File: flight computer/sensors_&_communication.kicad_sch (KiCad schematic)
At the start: 30 parts, among them IC2 114993390, IC3 ADXL375BCCZ-RL, J22 SMA-J-P-H-ST-EM1, J23 SMA-J-P-H-ST-EM1, U10 MAX-M10S-00B, U8 BMP581, U9 BNO086

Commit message: General progress on the PCB
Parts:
- C42, C43, C44, C45, C46, C47, C48, C49, C50, C51, C52, C53, C54: footprint Capacitor_SMD:C_0805_2012Metric_Pad1.18x1.45mm_HandSolder -> Capacitor_SMD:C_0603_1608Metric_Pad1.08x0.95mm_HandSolder
- R39, R40, R41, R42, R43, R44: footprint Resistor_SMD:R_0805_2012Metric_Pad1.20x1.40mm_HandSolder -> Resistor_SMD:R_0603_1608Metric_Pad0.98x0.95mm_HandSolder
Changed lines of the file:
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@@
 			)
 		)
-		(property "Footprint" "Capacitor_SMD:C_0805_2012Metric_Pad1.18x1.45mm_HandSolder"
+		(property "Footprint" "Capacitor_SMD:C_0603_1608Metric_Pad1.08x0.95mm_HandSolder"
 			(at 162.2552 53.34 0)
 			(hide yes)
@@
 			)
 		)
-		(property "Footprint" "Capacitor_SMD:C_0805_2012Metric_Pad1.18x1.45mm_HandSolder"
+		(property "Footprint" "Capacitor_SMD:C_0603_1608Metric_Pad1.08x0.95mm_HandSolder"
 			(at 131.1148 38.1 0)
 			(hide yes)
@@
 			)
 		)
-		(property "Footprint" "Resistor_SMD:R_0805_2012Metric_Pad1.20x1.40mm_HandSolder"
+		(property "Footprint" "Resistor_SMD:R_0603_1608Metric_Pad0.98x0.95mm_HandSolder"
 			(at 33.02 41.148 90)
 			(hide yes)
@@
 			)
 		)
-		(property "Footprint" "Capacitor_SMD:C_0805_2012Metric_Pad1.18x1.45mm_HandSolder"
+		(property "Footprint" "Capacitor_SMD:C_0603_1608Metric_Pad1.08x0.95mm_HandSolder"
 			(at 119.6848 38.1 0)
 			(hide yes)
@@
 			)
 		)
-		(property "Footprint" "Resistor_SMD:R_0805_2012Metric_Pad1.20x1.40mm_HandSolder"
+		(property "Footprint" "Resistor_SMD:R_0603_1608Metric_Pad0.98x0.95mm_HandSolder"
 			(at 67.31 136.652 90)
 			(hide yes)
@@
 			)
 		)
-		(property "Footprint" "Capacitor_SMD:C_0805_2012Metric_Pad1.18x1.45mm_HandSolder"
+		(property "Footprint" "Capacitor_SMD:C_0603_1608Metric_Pad1.08x0.95mm_HandSolder"
 			(at 173.6852 53.34 0)
 			(hide yes)
@@
 			)
 		)
-		(property "Footprint" "Resistor_SMD:R_0805_2012Metric_Pad1.20x1.40mm_HandSolder"
+		(property "Footprint" "Resistor_SMD:R_0603_1608Metric_Pad0.98x0.95mm_HandSolder"
 			(at 33.02 43.688 90)
 			(hide yes)
@@
 			)
 		)
-		(property "Footprint" "Capacitor_SMD:C_0805_2012Metric_Pad1.18x1.45mm_HandSolder"
+		(property "Footprint" "Capacitor_SMD:C_0603_1608Metric_Pad1.08x0.95mm_HandSolder"
 			(at 98.7552 63.5 0)
 			(hide yes)
@@
 			)
 		)
-		(property "Footprint" "Resistor_SMD:R_0805_2012Metric_Pad1.20x1.40mm_HandSolder"
+		(property "Footprint" "Resistor_SMD:R_0603_1608Metric_Pad0.98x0.95mm_HandSolder"
 			(at 101.6 46.482 90)
 			(hide yes)
@@
 			)
 		)
-		(property "Footprint" "Capacitor_SMD:C_0805_2012Metric_Pad1.18x1.45mm_HandSolder"
+		(property "Footprint" "Capacitor_SMD:C_0603_1608Metric_Pad1.08x0.95mm_HandSolder"
 			(at 177.4952 101.6 0)
 			(hide yes)
@@
 			)
 		)
-		(property "Footprint" "Capacitor_SMD:C_0805_2012Metric_Pad1.18x1.45mm_HandSolder"
+		(property "Footprint" "Capacitor_SMD:C_0603_1608Metric_Pad1.08x0.95mm_HandSolder"
 			(at 23.1648 97.79 0)
 			(hide yes)
@@
 			)
 		)
-		(property "Footprint" "Capacitor_SMD:C_0805_2012Metric_Pad1.18x1.45mm_HandSolder"
+		(property "Footprint" "Capacitor_SMD:C_0603_1608Metric_Pad1.08x0.95mm_HandSolder"
 			(at 82.2452 97.79 0)
 			(hide yes)
@@
 			)
 		)
-		(property "Footprint" "Resistor_SMD:R_0805_2012Metric_Pad1.20x1.40mm_HandSolder"
+		(property "Footprint" "Resistor_SMD:R_0603_1608Metric_Pad0.98x0.95mm_HandSolder"
 			(at 101.6 41.148 90)
 			(hide yes)
@@
 			)
 		)
-		(property "Footprint" "Capacitor_SMD:C_0805_2012Metric_Pad1.18x1.45mm_HandSolder"
+		(property "Footprint" "Capacitor_SMD:C_0603_1608Metric_Pad1.08x0.95mm_HandSolder"
 			(at 164.7952 101.6 0)
 			(hide yes)
@@
 			)
 		)
-		(property "Footprint" "Capacitor_SMD:C_0805_2012Metric_Pad1.18x1.45mm_HandSolder"
+		(property "Footprint" "Capacitor_SMD:C_0603_1608Metric_Pad1.08x0.95mm_HandSolder"
 			(at 51.7652 146.05 0)
 			(hide yes)
@@
 			)
 		)
-		(property "Footprint" "Capacitor_SMD:C_0805_2012Metric_Pad1.18x1.45mm_HandSolder"
+		(property "Footprint" "Capacitor_SMD:C_0603_1608Metric_Pad1.08x0.95mm_HandSolder"
 			(at 94.9452 97.79 0)
 			(hide yes)
@@
 			)
 		)
-		(property "Footprint" "Capacitor_SMD:C_0805_2012Metric_Pad1.18x1.45mm_HandSolder"
+		(property "Footprint" "Capacitor_SMD:C_0603_1608Metric_Pad1.08x0.95mm_HandSolder"
 			(at 108.2548 38.1 0)
 			(hide yes)
@@
 			)
 		)
-		(property "Footprint" "Capacitor_SMD:C_0805_2012Metric_Pad1.18x1.45mm_HandSolder"
+		(property "Footprint" "Capacitor_SMD:C_0603_1608Metric_Pad1.08x0.95mm_HandSolder"
 			(at 150.8252 53.34 0)
 			(hide yes)
@@
 			)
 		)
-		(property "Footprint" "Resistor_SMD:R_0805_2012Metric_Pad1.20x1.40mm_HandSolder"
+		(property "Footprint" "Resistor_SMD:R_0603_1608Metric_Pad0.98x0.95mm_HandSolder"
 			(at 33.02 38.608 90)
 			(hide yes)

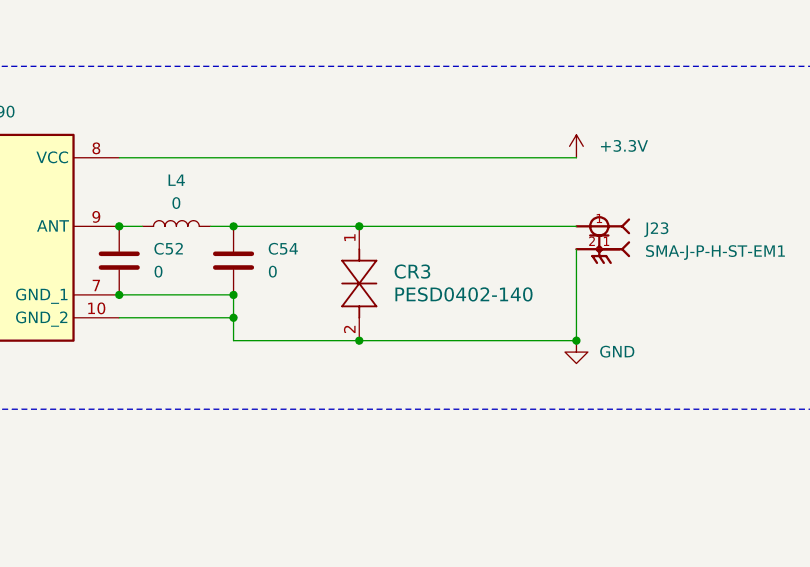
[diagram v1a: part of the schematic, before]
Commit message: Microcontroller power complete
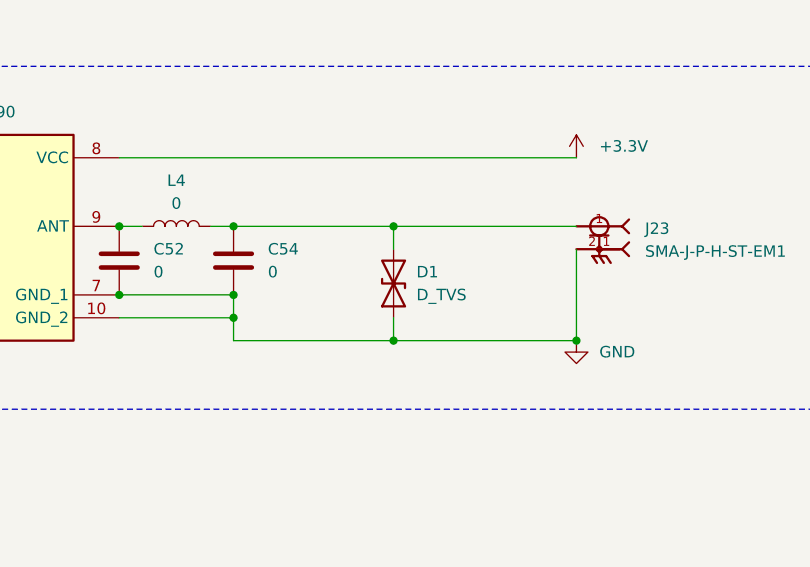
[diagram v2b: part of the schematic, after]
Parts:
- removed CR3: PESD0402-140, Inductor_SMD:L_0402_1005Metric_Pad0.77x0.64mm_HandSolder, symbol Snapeda:PESD0402-140
- added D1: D_TVS, Diode_SMD:D_0603_1608Metric_Pad1.05x0.95mm_HandSolder, symbol Device:D_TVS
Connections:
- net GND: now also D1.1 (A1)
- net at C54.1, J23.1, L4.2: now also D1.2 (A2)
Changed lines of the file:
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@@
 	)
 	(junction
-		(at 190.5 106.68)
-		(diameter 0)
-		(color 0 0 0 0)
-	)
-	(junction
 		(at 124.46 165.1)
 		(diameter 0)
@@
 	)
 	(junction
-		(at 190.5 93.98)
-		(diameter 0)
-		(color 0 0 0 0)
-	)
-	(junction
 		(at 21.59 137.16)
 		(diameter 0)
@@
 	)
 	(junction
+		(at 194.31 106.68)
+		(diameter 0)
+		(color 0 0 0 0)
+	)
+	(junction
 		(at 149.86 43.18)
 		(diameter 0)
@@
 	)
 	(junction
+		(at 194.31 93.98)
+		(diameter 0)
+		(color 0 0 0 0)
+	)
+	(junction
 		(at 109.22 30.48)
 		(diameter 0)
@@
 		)
 	)
+	(wire
+		(pts
+			(xy 194.31 104.14) (xy 194.31 106.68)
+		)
+		(stroke
+			(width 0)
+			(type default)
+		)
+	)
 	(polyline
 		(pts
@@
 	(wire
 		(pts
+			(xy 194.31 93.98) (xy 194.31 96.52)
+		)
+		(stroke
+			(width 0)
+			(type default)
+		)
+	)
+	(wire
+		(pts
 			(xy 248.92 45.72) (xy 233.68 45.72)
 		)
@@
 	(wire
 		(pts
-			(xy 190.5 106.68) (xy 214.63 106.68)
+			(xy 176.53 106.68) (xy 194.31 106.68)
 		)
 		(stroke
@@
 		)
 	)
+	(wire
+		(pts
+			(xy 194.31 93.98) (xy 214.63 93.98)
+		)
+		(stroke
+			(width 0)
+			(type default)
+		)
+	)
 	(polyline
 		(pts
@@
 	(wire
 		(pts
-			(xy 176.53 93.98) (xy 190.5 93.98)
+			(xy 176.53 93.98) (xy 194.31 93.98)
 		)
 		(stroke
@@
 	(wire
 		(pts
+			(xy 194.31 106.68) (xy 214.63 106.68)
+		)
+		(stroke
+			(width 0)
+			(type default)
+		)
+	)
+	(wire
+		(pts
 			(xy 24.13 41.91) (xy 29.21 41.91)
 		)
@@
 		)
 	)
-	(wire
-		(pts
-			(xy 190.5 93.98) (xy 214.63 93.98)
-		)
-		(stroke
-			(width 0)
-			(type default)
-		)
-	)
 	(polyline
 		(pts
@@
 		)
 	)
-	(wire
-		(pts
-			(xy 176.53 106.68) (xy 190.5 106.68)
-		)
-		(stroke
-			(width 0)
-			(type default)
-		)
-	)
 	(polyline
 		(pts
@@
 	)
 	(symbol
-		(lib_id "Snapeda:PESD0402-140")
-		(at 190.5 106.68 90)
+		(lib_id "Device:D_TVS")
+		(at 194.31 100.33 90)
 		(unit 1)
 		(body_style 1)
@@
 		(dnp no)
 		(fields_autoplaced yes)
-		(property "Reference" "CR3"
-			(at 194.31 99.0599 90)
+		(property "Reference" "D1"
+			(at 196.85 99.0599 90)
 			(show_name no)
 			(do_not_autoplace no)
 			(effects
 				(font
-					(size 1.524 1.524)
+					(size 1.27 1.27)
 				)
 				(justify right)
 			)
 		)
-		(property "Value" "PESD0402-140"
-			(at 194.31 101.5999 90)
+		(property "Value" "D_TVS"
+			(at 196.85 101.5999 90)
 			(show_name no)
 			(do_not_autoplace no)
 			(effects
 				(font
-					(size 1.524 1.524)
+					(size 1.27 1.27)
 				)
 				(justify right)
 			)
 		)
-		(property "Footprint" "Inductor_SMD:L_0402_1005Metric_Pad0.77x0.64mm_HandSolder"
-			(at 194.31 101.5999 90)
+		(property "Footprint" "Diode_SMD:D_0603_1608Metric_Pad1.05x0.95mm_HandSolder"
+			(at 194.31 100.33 0)
 			(hide yes)
-			(show_name yes)
+			(show_name no)
 			(do_not_autoplace no)
 			(effects
@@
 					(size 1.27 1.27)
 				)
-				(justify right)
 			)
 		)
-		(property "Datasheet" "PESD0402-140"
-			(at 194.31 104.1399 90)
+		(property "Datasheet" ""
+			(at 194.31 100.33 0)
 			(hide yes)
-			(show_name yes)
+			(show_name no)
 			(do_not_autoplace no)
 			(effects
@@
 					(size 1.27 1.27)
 				)
-				(justify right)
 			)
 		)
-		(property "Description" ""
-			(at 190.5 106.68 0)
+		(property "Description" "Bidirectional transient-voltage-suppression diode"
+			(at 194.31 100.33 0)
 			(hide yes)
-			(show_name yes)
+			(show_name no)
 			(do_not_autoplace no)
 			(effects
@@
 			(project "flight computer"
 				(path "/bdd95a45-8144-4be4-bdb0-261aee7edef2"
-					(reference "CR3")
+					(reference "D1")
 					(unit 1)
 				)

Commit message: Designed RF segment
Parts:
- removed CR2: PESD0402-140, Diode_SMD:D_0402_1005Metric_Pad0.77x0.64mm_HandSolder, symbol Snapeda:PESD0402-140
- added D2: D_TVS, Diode_SMD:D_0603_1608Metric_Pad1.05x0.95mm_HandSolder, symbol Device:D_TVS
- L3: footprint Inductor_SMD:L_0402_1005Metric_Pad0.77x0.64mm_HandSolder -> Inductor_SMD:L_0603_1608Metric_Pad1.05x0.95mm_HandSolder
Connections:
- net GND: now also D2.1 (A1)
- net at J22.1, L3.1, U10.11 (RF_IN): now also D2.2 (A2)
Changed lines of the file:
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@@
 	)
 	(junction
-		(at 124.46 165.1)
-		(diameter 0)
-		(color 0 0 0 0)
-	)
-	(junction
-		(at 25.4 124.46)
+		(at 50.8 146.05)
 		(diameter 0)
 		(color 0 0 0 0)
 	)
 	(junction
-		(at 21.59 137.16)
+		(at 124.46 165.1)
 		(diameter 0)
 		(color 0 0 0 0)
@@
 	)
 	(junction
+		(at 39.37 124.46)
+		(diameter 0)
+		(color 0 0 0 0)
+	)
+	(junction
 		(at 24.13 97.79)
 		(diameter 0)
@@
 	(wire
 		(pts
-			(xy 21.59 137.16) (xy 25.4 137.16)
-		)
-		(stroke
-			(width 0)
-			(type default)
-		)
-	)
-	(wire
-		(pts
 			(xy 77.47 97.79) (xy 77.47 95.25)
 		)
@@
 	(wire
 		(pts
-			(xy 17.78 137.16) (xy 21.59 137.16)
-		)
-		(stroke
-			(width 0)
-			(type default)
-		)
-	)
-	(wire
-		(pts
 			(xy 97.79 63.5) (xy 97.79 66.04)
 		)
@@
 	(wire
 		(pts
-			(xy 20.32 124.46) (xy 25.4 124.46)
+			(xy 27.94 90.17) (xy 27.94 92.71)
 		)
 		(stroke
@@
 	(wire
 		(pts
-			(xy 27.94 90.17) (xy 27.94 92.71)
+			(xy 77.47 97.79) (xy 81.28 97.79)
 		)
 		(stroke
@@
 	(wire
 		(pts
-			(xy 77.47 97.79) (xy 81.28 97.79)
+			(xy 111.76 86.36) (xy 130.81 86.36)
 		)
 		(stroke
@@
 	(wire
 		(pts
-			(xy 111.76 86.36) (xy 130.81 86.36)
+			(xy 173.99 93.98) (xy 176.53 93.98)
 		)
 		(stroke
@@
 	(wire
 		(pts
-			(xy 173.99 93.98) (xy 176.53 93.98)
+			(xy 39.37 124.46) (xy 50.8 124.46)
 		)
 		(stroke
@@
 		)
 	)
+	(wire
+		(pts
+			(xy 39.37 130.81) (xy 39.37 124.46)
+		)
+		(stroke
+			(width 0)
+			(type default)
+		)
+	)
 	(polyline
 		(pts
@@
 	(wire
 		(pts
-			(xy 25.4 124.46) (xy 50.8 124.46)
+			(xy 20.32 124.46) (xy 39.37 124.46)
 		)
 		(stroke
@@
 	(wire
 		(pts
+			(xy 39.37 146.05) (xy 50.8 146.05)
+		)
+		(stroke
+			(width 0)
+			(type default)
+		)
+	)
+	(wire
+		(pts
 			(xy 124.46 161.29) (xy 124.46 165.1)
 		)
@@
 	(wire
 		(pts
-			(xy 97.79 30.48) (xy 105.41 30.48)
+			(xy 39.37 138.43) (xy 39.37 146.05)
 		)
 		(stroke
@@
 	(wire
 		(pts
-			(xy 161.29 45.72) (xy 161.29 43.18)
+			(xy 97.79 30.48) (xy 105.41 30.48)
 		)
 		(stroke
@@
 	(wire
 		(pts
-			(xy 17.78 137.16) (xy 17.78 124.46)
+			(xy 161.29 45.72) (xy 161.29 43.18)
 		)
 		(stroke
@@
 	)
 	(symbol
+		(lib_id "power:GND")
+		(at 17.78 124.46 0)
+		(unit 1)
+		(body_style 1)
+		(exclude_from_sim no)
+		(in_bom yes)
+		(on_board yes)
+		(in_pos_files yes)
+		(dnp no)
+		(fields_autoplaced yes)
+		(property "Reference" "#PWR0119"
+			(at 17.78 130.81 0)
+			(hide yes)
+			(show_name no)
+			(do_not_autoplace no)
+			(effects
+				(font
+					(size 1.27 1.27)
+				)
+			)
+		)
+		(property "Value" "GND"
+			(at 17.78 129.54 0)
+			(show_name no)
+			(do_not_autoplace no)
+			(effects
+				(font
+					(size 1.27 1.27)
+				)
+			)
+		)
+		(property "Footprint" ""
+			(at 17.78 124.46 0)
+			(hide yes)
+			(show_name no)
+			(do_not_autoplace no)
+			(effects
+				(font
+					(size 1.27 1.27)
+				)
+			)
+		)
+		(property "Datasheet" ""
+			(at 17.78 124.46 0)
+			(hide yes)
+			(show_name no)
+			(do_not_autoplace no)
+			(effects
+				(font
+					(size 1.27 1.27)
+				)
+			)
+		)
+		(property "Description" "Power symbol creates a global label with name \"GND\" , ground"
+			(at 17.78 124.46 0)
+			(hide yes)
+			(show_name no)
+			(do_not_autoplace no)
+			(effects
+				(font
+					(size 1.27 1.27)
+				)
+			)
+		)
+		(pin "1"
+		)
+		(instances
+			(project "flight computer"
+				(path "/bdd95a45-8144-4be4-bdb0-261aee7edef2"
+					(reference "#PWR0119")
+					(unit 1)
+				)
+			)
+		)
+	)
+	(symbol
 		(lib_id "Samacsys:114993390")
 		(at 130.81 86.36 0)
@@
 			)
 		)
-		(property "Footprint" "Inductor_SMD:L_0402_1005Metric_Pad0.77x0.64mm_HandSolder"
+		(property "Footprint" "Inductor_SMD:L_0603_1608Metric_Pad1.05x0.95mm_HandSolder"
 			(at 50.8 132.08 0)
 			(hide yes)
@@
 	)
 	(symbol
-		(lib_id "Snapeda:PESD0402-140")
-		(at 25.4 137.16 90)
+		(lib_id "power:GND")
+		(at 149.86 55.88 0)
 		(unit 1)
 		(body_style 1)
@@
 		(dnp no)
 		(fields_autoplaced yes)
-		(property "Reference" "CR2"
-			(at 29.21 129.5399 90)
+		(property "Reference" "#PWR0116"
+			(at 149.86 62.23 0)
+			(hide yes)
 			(show_name no)
 			(do_not_autoplace no)
 			(effects
 				(font
-					(size 1.524 1.524)
+					(size 1.27 1.27)
 				)
-				(justify right)
 			)
 		)
-		(property "Value" "PESD0402-140"
-			(at 29.21 132.0799 90)
+		(property "Value" "GND"
+			(at 147.32 57.1499 0)
 			(show_name no)
 			(do_not_autoplace no)
 			(effects
 				(font
-					(size 1.524 1.524)
+					(size 1.27 1.27)
 				)
 				(justify right)
 			)
 		)
-		(property "Footprint" "Diode_SMD:D_0402_1005Metric_Pad0.77x0.64mm_HandSolder"
-			(at 29.21 132.0799 90)
+		(property "Footprint" ""
+			(at 149.86 55.88 0)
 			(hide yes)
-			(show_name yes)
+			(show_name no)
 			(do_not_autoplace no)
 			(effects
@@
 					(size 1.27 1.27)
 				)
-				(justify right)
 			)
 		)
-		(property "Datasheet" "PESD0402-140"
-			(at 29.21 134.6199 90)
+		(property "Datasheet" ""
+			(at 149.86 55.88 0)
 			(hide yes)
-			(show_name yes)
+			(show_name no)
 			(do_not_autoplace no)
 			(effects
@@
 					(size 1.27 1.27)
 				)
-				(justify right)
 			)
 		)
-		(property "Description" ""
-			(at 25.4 137.16 0)
+		(property "Description" "Power symbol creates a global label with name \"GND\" , ground"
+			(at 149.86 55.88 0)
 			(hide yes)
-			(show_name yes)
+			(show_name no)
 			(do_not_autoplace no)
 			(effects
@@
 		(pin "1"
 		)
-		(pin "2"
-		)
 		(instances
 			(project "flight computer"
 				(path "/bdd95a45-8144-4be4-bdb0-261aee7edef2"
-					(reference "CR2")
+					(reference "#PWR0116")
 					(unit 1)
 				)
@@
 	)
 	(symbol
-		(lib_id "power:GND")
-		(at 149.86 55.88 0)
+		(lib_id "Device:D_TVS")
+		(at 39.37 134.62 90)
 		(unit 1)
 		(body_style 1)
@@
 		(dnp no)
 		(fields_autoplaced yes)
-		(property "Reference" "#PWR0116"
-			(at 149.86 62.23 0)
-			(hide yes)
+		(property "Reference" "D2"
+			(at 41.91 133.3499 90)
 			(show_name no)
 			(do_not_autoplace no)
@@
 					(size 1.27 1.27)
 				)
+				(justify right)
 			)
 		)
-		(property "Value" "GND"
-			(at 147.32 57.1499 0)
+		(property "Value" "D_TVS"
+			(at 41.91 135.8899 90)
 			(show_name no)
 			(do_not_autoplace no)
@@
 			)
 		)
-		(property "Footprint" ""
-			(at 149.86 55.88 0)
+		(property "Footprint" "Diode_SMD:D_0603_1608Metric_Pad1.05x0.95mm_HandSolder"
+			(at 39.37 134.62 0)
 			(hide yes)
 			(show_name no)
@@
 		)
 		(property "Datasheet" ""
-			(at 149.86 55.88 0)
+			(at 39.37 134.62 0)
 			(hide yes)
 			(show_name no)
@@
 			)
 		)
-		(property "Description" "Power symbol creates a global label with name \"GND\" , ground"
-			(at 149.86 55.88 0)
+		(property "Description" "Bidirectional transient-voltage-suppression diode"
+			(at 39.37 134.62 0)
 			(hide yes)
 			(show_name no)
@@
 		(pin "1"
 		)
+		(pin "2"
+		)
 		(instances
 			(project "flight computer"
 				(path "/bdd95a45-8144-4be4-bdb0-261aee7edef2"
-					(reference "#PWR0116")
+					(reference "D2")
 					(unit 1)
 				)
@@
 					(unit 1)
 				)
-			)
-		)
-	)
-	(symbol
-		(lib_id "power:GND")
-		(at 21.59 137.16 0)
-		(unit 1)
-		(body_style 1)
-		(exclude_from_sim no)
-		(in_bom yes)
-		(on_board yes)
-		(in_pos_files yes)
-		(dnp no)
-		(fields_autoplaced yes)
-		(property "Reference" "#PWR0103"
-			(at 21.59 143.51 0)
-			(hide yes)
-			(show_name no)
-			(do_not_autoplace no)
-			(effects
-				(font
-					(size 1.27 1.27)
-				)
-			)
-		)
-		(property "Value" "GND"
-			(at 21.59 142.24 0)
-			(show_name no)
-			(do_not_autoplace no)
-			(effects
-				(font
-					(size 1.27 1.27)
-				)
-			)
-		)
-		(property "Footprint" ""
-			(at 21.59 137.16 0)
-			(hide yes)
-			(show_name no)
-			(do_not_autoplace no)
-			(effects
-				(font
-					(size 1.27 1.27)
-				)
-			)
-		)
-		(property "Datasheet" ""
-			(at 21.59 137.16 0)
-			(hide yes)
-			(show_name no)
-			(do_not_autoplace no)
-			(effects
-				(font
-					(size 1.27 1.27)
-				)
-			)
-		)
-		(property "Description" "Power symbol creates a global label with name \"GND\" , ground"
-			(at 21.59 137.16 0)
-			(hide yes)
-			(show_name no)
-			(do_not_autoplace no)
-			(effects
-				(font
-					(size 1.27 1.27)
-				)
-			)
-		)
-		(pin "1"
-		)
-		(instances
-			(project "flight computer"
-				(path "/bdd95a45-8144-4be4-bdb0-261aee7edef2"
-					(reference "#PWR0103")
-					(unit 1)
-				)

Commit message: Final few traces
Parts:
- C43: value 0.1uF -> 10nF
- L3: value L -> 27nH
- R42: value 0 -> 10
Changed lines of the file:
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@@
 			)
 		)
-		(property "Value" "0"
+		(property "Value" "10"
 			(at 67.31 134.62 90)
 			(show_name no)
@@
 			)
 		)
-		(property "Value" "L"
+		(property "Value" "27nH"
 			(at 52.07 133.3499 0)
 			(show_name no)
@@
 			)
 		)
-		(property "Value" "0.1uF"
+		(property "Value" "10nF"
 			(at 54.61 143.5099 0)
 			(show_name no)
